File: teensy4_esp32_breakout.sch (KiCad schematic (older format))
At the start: 16 parts, among them J1 Conn_01x08, J2 Conn_02x05_Odd_Even, SW1 ON_OFF, U1 ESP32-WROOM-32D, U2 TLV75533PDBV

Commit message: Forgot to save
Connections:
- no-connect marks 21 -> 23
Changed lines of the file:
@@
 NoConn ~ 6250 4800
 NoConn ~ 6250 4900
+NoConn ~ 3950 1500
+NoConn ~ 3050 2850
 $EndSCHEMATC

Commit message: fix regulator part number
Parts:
- U2: value TLV75533PDBV -> TLV75733PDBVR
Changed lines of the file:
@@
 EESchema Schematic File Version 4
+LIBS:teensy4_esp32_breakout-cache
 EELAYER 30 0
 EELAYER END
@@
 P 8950 3750
 F 0 "U2" H 8950 4092 50  0000 C CNN
-F 1 "TLV75533PDBV" H 8950 4001 50  0000 C CNN
+F 1 "TLV75733PDBVR" H 8950 4001 50  0000 C CNN
 F 2 "Package_TO_SOT_SMD:SOT-23-5" H 8950 4050 50  0001 C CIN
 F 3 "http://www.ti.com/lit/ds/symlink/tlv755p.pdf" H 8950 3750 50  0001 C CNN

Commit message: Added two more pins from ESP32 to header, including pin used for ESP_BUSY by WiFiNINA
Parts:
- removed J2: Conn_02x05_Odd_Even, Connector_PinHeader_2.54mm:PinHeader_2x05_P2.54mm_Vertical, symbol Connector_Generic:Conn_02x05_Odd_Even
- added J2: Conn_02x06_Odd_Even, Connector_PinHeader_2.54mm:PinHeader_2x06_P2.54mm_Vertical, symbol Connector_Generic:Conn_02x06_Odd_Even
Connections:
- net +3V3: now also J2.2 (Pin_2)
- net +5V: now also J2.4 (Pin_4)
- net CS: now also J2.5 (Pin_5)
- net GND: now also J2.1 (Pin_1)
- net IO25: now also J2.6 (Pin_6)
- net IO26: now also J2.8 (Pin_8)
- net IO27: now also J2.10 (Pin_10)
- net MISO: now also J2.9 (Pin_9)
- net MOSI: now also J2.7 (Pin_7)
- net SCK: now also J2.3 (Pin_3)
- net ESP_BUSY: now reaches U1.8 (IO32)
- net ESP_BUSY: now also J2.11 (Pin_11)
- net IO33: now reaches U1.9 (IO33)
- net IO33: now also J2.12 (Pin_12)
- no-connect marks 23 -> 22
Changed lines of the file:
@@
-	1    0    0    -1
-$EndComp
-$Comp
-L Connector_Generic:Conn_02x05_Odd_Even J2
-U 1 1 5D8EE5FE
-P 7650 3350
-F 0 "J2" H 7700 3767 50  0000 C CNN
-F 1 "Conn_02x05_Odd_Even" H 7700 3676 50  0000 C CNN
-F 2 "Connector_PinHeader_2.54mm:PinHeader_2x05_P2.54mm_Vertical" H 7650 3350 50  0001 C CNN
-F 3 "~" H 7650 3350 50  0001 C CNN
-	1    7650 3350
 	1    0    0    -1
 $EndComp
@@
 $EndComp
 $Comp
-L power:PWR_FLAG #FLG0101
-U 1 1 5D8F83F8
-P 4750 3650
-F 0 "#FLG0101" H 4750 3725 50  0001 C CNN
-F 1 "PWR_FLAG" H 4750 3823 50  0000 C CNN
-F 2 "" H 4750 3650 50  0001 C CNN
-F 3 "~" H 4750 3650 50  0001 C CNN
-	1    4750 3650
-	-1   0    0    1
-$EndComp
-Connection ~ 4750 3650
-$Comp
 L power:PWR_FLAG #FLG0102
 U 1 1 5D8F97B5
@@
 	1    0    0    -1
 $EndComp
-Wire Wire Line
-	7950 3250 8300 3250
 Wire Wire Line
 	8300 3250 8300 3650
@@
 Text Label 7950 3450 0    50   ~ 0
 IO26
-Text Label 7950 3550 0    50   ~ 0
-IO27
 Text Label 6250 4300 0    50   ~ 0
 IO25
 Text Label 6250 4400 0    50   ~ 0
 IO26
-Text Label 6250 4500 0    50   ~ 0
-IO27
 NoConn ~ 6250 3000
 NoConn ~ 6250 3200
@@
 NoConn ~ 6250 3900
 NoConn ~ 6250 4000
-NoConn ~ 6250 4600
-NoConn ~ 6250 4700
 NoConn ~ 6250 4800
 NoConn ~ 6250 4900
 NoConn ~ 3950 1500
 NoConn ~ 3050 2850
+Text Label 6250 4600 0    50   ~ 0
+ESP_BUSY
+Text Label 6250 4500 0    50   ~ 0
+IO27
+Text Label 7950 3550 0    50   ~ 0
+IO27
+Text Label 7450 3650 2    50   ~ 0
+ESP_BUSY
+$Comp
+L Connector_Generic:Conn_02x06_Odd_Even J2
+U 1 1 5D8DD515
+P 7650 3350
+F 0 "J2" H 7700 3767 50  0000 C CNN
+F 1 "Conn_02x06_Odd_Even" H 7700 3676 50  0000 C CNN
+F 2 "Connector_PinHeader_2.54mm:PinHeader_2x06_P2.54mm_Vertical" H 7650 3350 50  0001 C CNN
+F 3 "~" H 7650 3350 50  0001 C CNN
+	1    7650 3350
+	1    0    0    -1
+$EndComp
+Wire Wire Line
+	7950 3250 8300 3250
+NoConn ~ 4450 3050
+Text Label 7950 3650 0    50   ~ 0
+IO33
+Text Label 6250 4700 0    50   ~ 0
+IO33
 $EndSCHEMATC

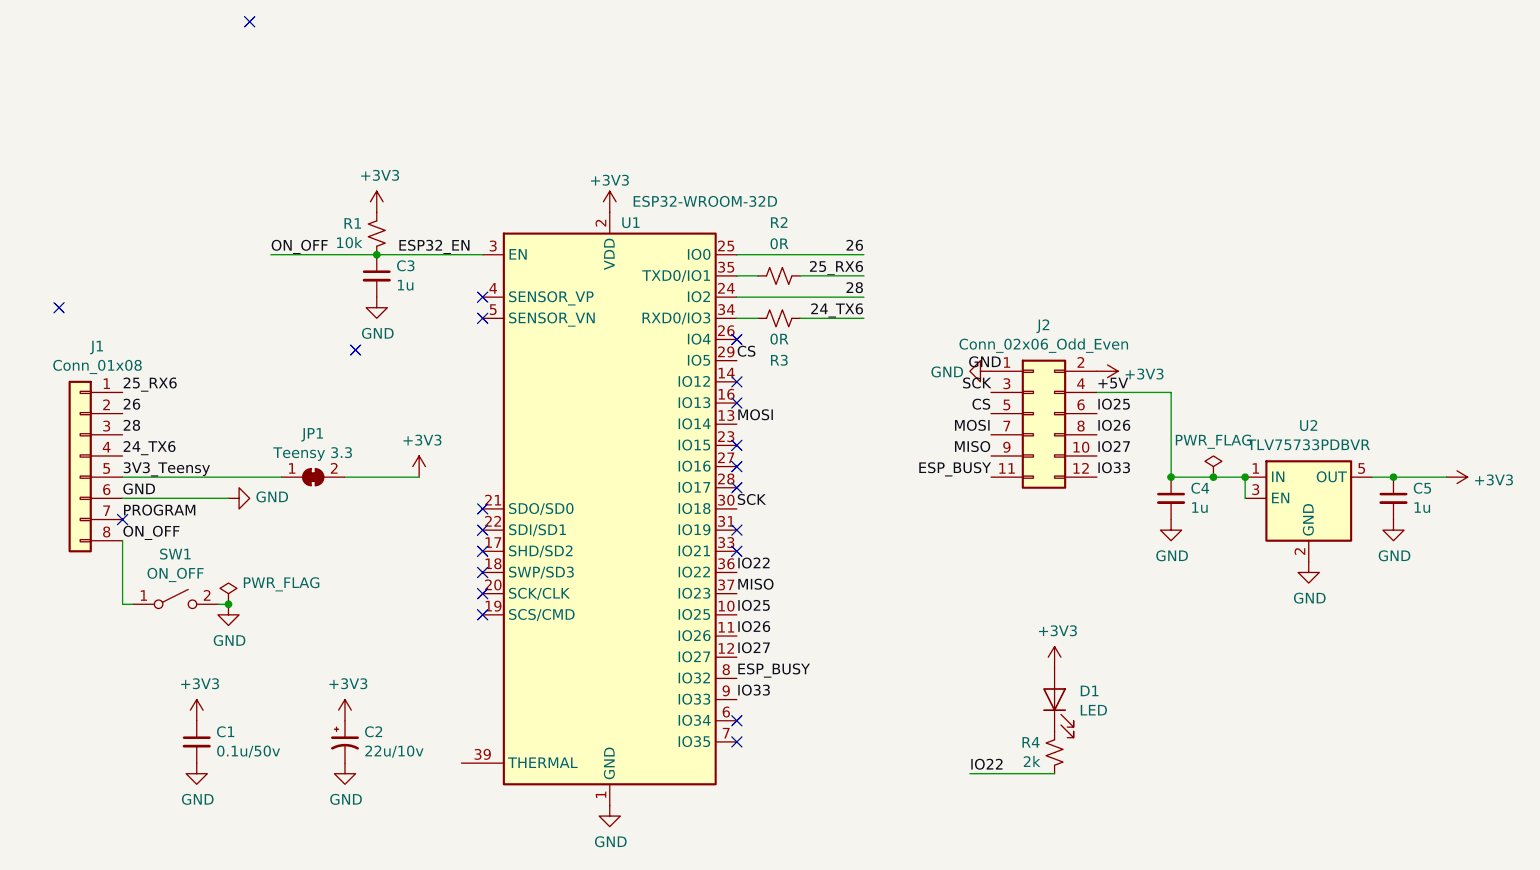
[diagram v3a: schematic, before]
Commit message: Updates to remove program/on_off pin connections
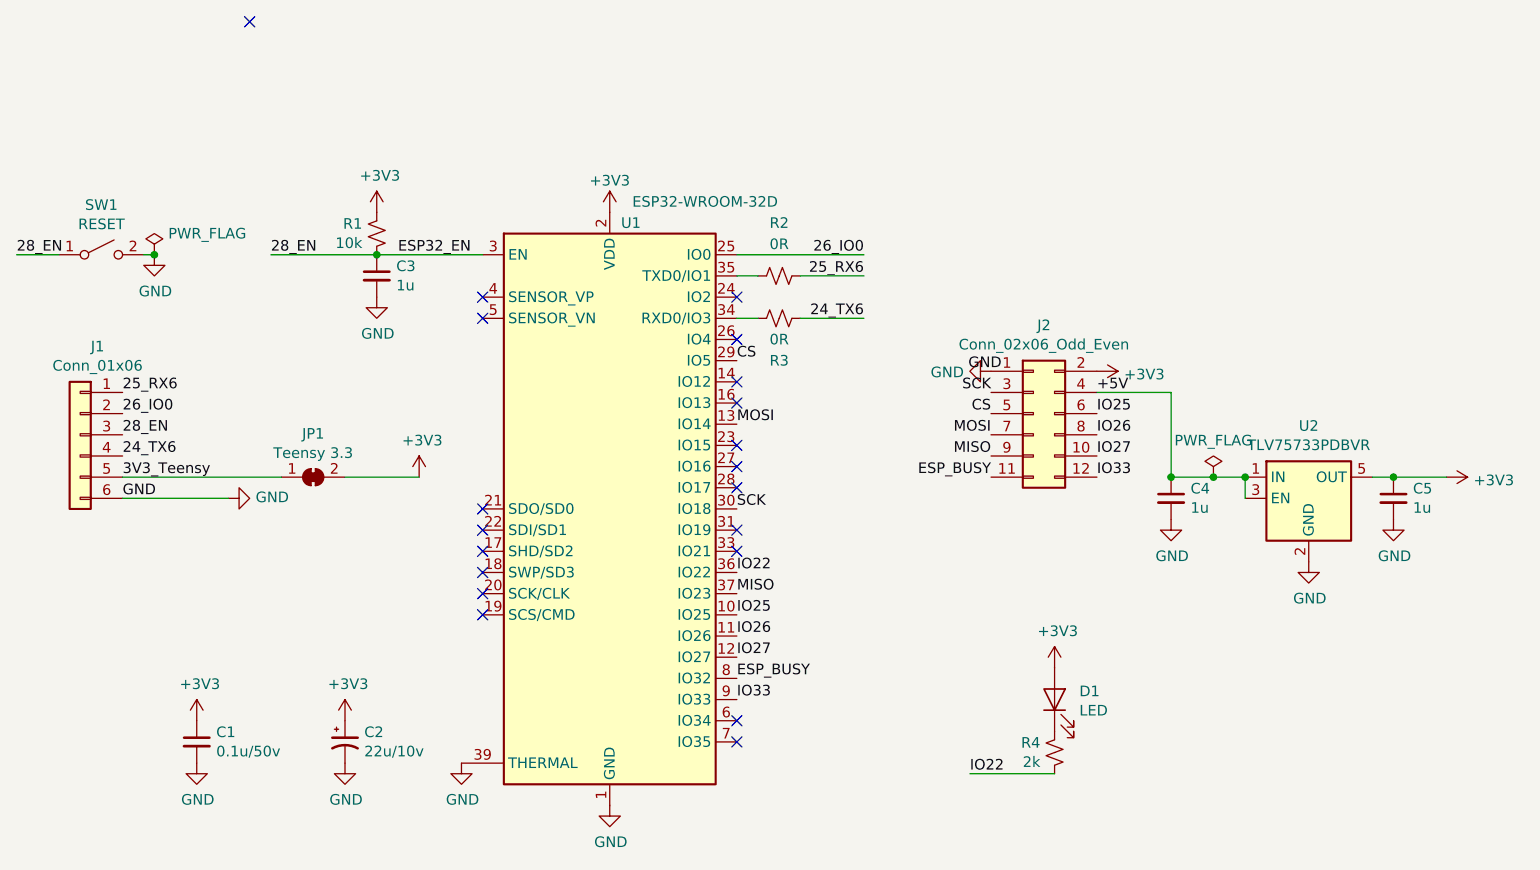
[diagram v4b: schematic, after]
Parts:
- removed J1: Conn_01x08, Connector_PinHeader_2.54mm:PinHeader_1x08_P2.54mm_Vertical, symbol Connector_Generic:Conn_01x08
- added J1: Conn_01x06, Connector_PinHeader_2.54mm:PinHeader_1x06_P2.54mm_Vertical, symbol Connector_Generic:Conn_01x06
- SW1: value ON_OFF -> RESET
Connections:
- net 24_TX6: now also J1.4 (Pin_4)
- net 25_RX6: now also J1.1 (Pin_1)
- net 3V3_Teensy: now also J1.5 (Pin_5)
- net GND: now also U1.39 (THERMAL), J1.6 (Pin_6)
- net 26 renamed 26_IO0
- net 26_IO0: now also J1.2 (Pin_2)
- net 28: no longer names the net of U1.24 (IO2)
- net ESP32_EN renamed 28_EN
- net 28_EN: now also J1.3 (Pin_3)
- no-connect marks 22 -> 20
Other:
- moved on the sheet: SW1
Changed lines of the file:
@@
 Comment4 ""
 $EndDescr
-$Comp
-L Connector_Generic:Conn_01x08 J1
-U 1 1 5D8AAC3C
-P 3150 3550
-F 0 "J1" H 3068 4067 50  0000 C CNN
-F 1 "Conn_01x08" H 3068 3976 50  0000 C CNN
-F 2 "Connector_PinHeader_2.54mm:PinHeader_1x08_P2.54mm_Vertical" H 3150 3550 50  0001 C CNN
-F 3 "~" H 3150 3550 50  0001 C CNN
-	1    3150 3550
-	-1   0    0    -1
-$EndComp
 Text Label 3350 3250 0    50   ~ 0
 25_RX6
 Text Label 3350 3350 0    50   ~ 0
-26
+26_IO0
 Text Label 3350 3450 0    50   ~ 0
-28
+28_EN
 Text Label 3350 3550 0    50   ~ 0
 24_TX6
@@
 Text Label 3350 3750 0    50   ~ 0
 GND
-Text Label 3350 3850 0    50   ~ 0
-PROGRAM
-Text Label 3350 3950 0    50   ~ 0
-ON_OFF
 $Comp
 L RF_Module:ESP32-WROOM-32D U1
@@
 	6250 2600 6850 2600
 Text Label 6850 2600 2    50   ~ 0
-26
-Wire Wire Line
-	6250 2800 6850 2800
-Text Label 6850 2800 2    50   ~ 0
-28
+26_IO0
 Text Label 4650 2600 0    50   ~ 0
 ESP32_EN
@@
 L Switch:SW_SPST SW1
 U 1 1 5D8B67A3
-P 3600 4250
-F 0 "SW1" H 3600 4485 50  0000 C CNN
-F 1 "ON_OFF" H 3600 4394 50  0000 C CNN
-F 2 "Button_Switch_SMD:Panasonic_EVQPUJ_EVQPUA" H 3600 4250 50  0001 C CNN
-F 3 "~" H 3600 4250 50  0001 C CNN
-	1    3600 4250
-	1    0    0    -1
-$EndComp
-Wire Wire Line
-	3400 4250 3350 4250
-Wire Wire Line
-	3350 3950 3350 4250
+P 3250 2600
+F 0 "SW1" H 3250 2835 50  0000 C CNN
+F 1 "RESET" H 3250 2744 50  0000 C CNN
+F 2 "Button_Switch_SMD:Panasonic_EVQPUJ_EVQPUA" H 3250 2600 50  0001 C CNN
+F 3 "~" H 3250 2600 50  0001 C CNN
+	1    3250 2600
+	1    0    0    -1
+$EndComp
 $Comp
 L power:GND #PWR0104
 U 1 1 5D8B7A2A
-P 3850 4250
-F 0 "#PWR0104" H 3850 4000 50  0001 C CNN
-F 1 "GND" H 3855 4077 50  0000 C CNN
-F 2 "" H 3850 4250 50  0001 C CNN
-F 3 "" H 3850 4250 50  0001 C CNN
-	1    3850 4250
-	1    0    0    -1
-$EndComp
-Wire Wire Line
-	3800 4250 3850 4250
+P 3500 2600
+F 0 "#PWR0104" H 3500 2350 50  0001 C CNN
+F 1 "GND" H 3505 2427 50  0000 C CNN
+F 2 "" H 3500 2600 50  0001 C CNN
+F 3 "" H 3500 2600 50  0001 C CNN
+	1    3500 2600
+	1    0    0    -1
+$EndComp
+Wire Wire Line
+	3450 2600 3500 2600
 NoConn ~ 5050 2800
 NoConn ~ 5050 2900
@@
 	1    0    0    -1
 $EndComp
-NoConn ~ 3350 3850
 $Comp
 L power:+3V3 #PWR0112
@@
 L power:PWR_FLAG #FLG0102
 U 1 1 5D8F97B5
-P 3850 4250
-F 0 "#FLG0102" H 3850 4325 50  0001 C CNN
-F 1 "PWR_FLAG" H 4100 4350 50  0000 C CNN
-F 2 "" H 3850 4250 50  0001 C CNN
-F 3 "~" H 3850 4250 50  0001 C CNN
-	1    3850 4250
+P 3500 2600
+F 0 "#FLG0102" H 3500 2675 50  0001 C CNN
+F 1 "PWR_FLAG" H 3750 2700 50  0000 C CNN
+F 2 "" H 3500 2600 50  0001 C CNN
+F 3 "~" H 3500 2600 50  0001 C CNN
+	1    3500 2600
 	1    0    0    -1
 $EndComp
 Wire Wire Line
 	3350 3750 3850 3750
-Connection ~ 3850 4250
+Connection ~ 3500 2600
 $Comp
 L Device:LED D1
@@
 Text Label 6250 3100 0    50   ~ 0
 CS
-Text Label 4050 2600 0    50   ~ 0
-ON_OFF
-Wire Wire Line
-	4050 2600 4550 2600
 $Comp
 L Regulator_Linear:TLV75533PDBV U2
@@
 NoConn ~ 6250 4900
 NoConn ~ 3950 1500
-NoConn ~ 3050 2850
 Text Label 6250 4600 0    50   ~ 0
 ESP_BUSY
@@
 Wire Wire Line
 	7950 3250 8300 3250
-NoConn ~ 4450 3050
 Text Label 7950 3650 0    50   ~ 0
 IO33
 Text Label 6250 4700 0    50   ~ 0
 IO33
+NoConn ~ 6250 2800
+Text Label 4050 2600 0    50   ~ 0
+28_EN
+$Comp
+L power:GND #PWR0119
+U 1 1 5D9B9624
+P 4950 5000
+F 0 "#PWR0119" H 4950 4750 50  0001 C CNN
+F 1 "GND" H 4955 4827 50  0000 C CNN
+F 2 "" H 4950 5000 50  0001 C CNN
+F 3 "" H 4950 5000 50  0001 C CNN
+	1    4950 5000
+	1    0    0    -1
+$EndComp
+Text Label 2850 2600 0    50   ~ 0
+28_EN
+Wire Wire Line
+	4050 2600 4550 2600
+Wire Wire Line
+	3050 2600 2850 2600
+$Comp
+L Connector_Generic:Conn_01x06 J1
+U 1 1 5DA1A5D0
+P 3150 3450
+F 0 "J1" H 3068 3867 50  0000 C CNN
+F 1 "Conn_01x06" H 3068 3776 50  0000 C CNN
+F 2 "Connector_PinHeader_2.54mm:PinHeader_1x06_P2.54mm_Vertical" H 3150 3450 50  0001 C CNN
+F 3 "~" H 3150 3450 50  0001 C CNN
+	1    3150 3450
+	-1   0    0    -1
+$EndComp
 $EndSCHEMATC
